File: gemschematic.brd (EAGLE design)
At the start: 90.2 x 61.9 mm, 57 parts, among them J1 USB, J3 QWIIC, J5 U.FL, Q1 2N3904, Q2 BSS138, Q3 MBT3904DW1T1, U1 ESP-WROOM-32NARROW, U2 AP2112K-3.3, U3 3.3V, U4 RFM96W, U5 CH340C, U6 BMP180, U7 STM32L073RZT6, X1 GPS_PA1010D

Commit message: Add files via upload
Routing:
- net GND: track 0.00 -> 423.1 mm, vias 0 -> 9
- net 3.3V: track 0.00 -> 279.9 mm
- net SDA: track 0.00 -> 189.3 mm, vias 0 -> 11
- net VCC: track 0.00 -> 183.9 mm, vias 0 -> 8
- net SCL: track 0.00 -> 179.1 mm, vias 0 -> 10
- net RESET: track 0.00 -> 171.9 mm, vias 0 -> 6
- net MISO: track 0.00 -> 156.4 mm, vias 0 -> 5
- net IO25: track 0.00 -> 154.6 mm, vias 0 -> 3
- net RFM_DIO2/32: track 0.00 -> 142.8 mm, vias 0 -> 2
- net SCK: track 0.00 -> 141.3 mm, vias 0 -> 7
- net IO27: track 0.00 -> 140.8 mm, vias 0 -> 5
- net ANT: track 0.00 -> 127.0 mm, vias 0 -> 5
- net MOSI: track 0.00 -> 125.1 mm, vias 0 -> 6
- net RXI: track 0.00 -> 120.5 mm, vias 0 -> 5
- net TXO: track 0.00 -> 114.0 mm, vias 0 -> 4
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
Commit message: Add files via upload
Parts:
- removed B1: (no value), microbuilder:CR1220-2
- removed C1: 0.1uF, microbuilder:0603-NO
- removed C2, C3: 10uF, microbuilder:0805-NO
- removed C4: 10uF, SparkFun-Capacitors:0603
- removed C5, C6: 0.1uF, SparkFun-Capacitors:0603
- removed C7, C8: 1.0uF, SparkFun-Capacitors:0603
- removed C9: 4.7uF, SparkFun-Capacitors:0603
- removed CONN3, CONN4: STEMMA_I2C_QT, microbuilder:JST_SH4
- removed D1: GREEN, microbuilder:CHIPLED_0603_NOOUTLINE
- removed D2: 1N4148, microbuilder:SOD-323
- removed D3: RED, microbuilder:CHIPLED_0603_NOOUTLINE
- removed D4: RED, SparkFun-LED:LED-0603
- removed D5: GREEN, SparkFun-LED:LED-0603
- removed FB1: FERRITE, microbuilder:0805-NO
- removed J1: USB, SparkFun-Connectors:USB-MICROB-PTH-MILL
- removed J3: QWIIC, SparkFun-Connectors:1X04_1MM_RA
- removed J4: (no value), SparkFun-Connectors:1X08_NO_SILK
- removed J5: U.FL, SparkFun-Connectors:U.FL
- removed J8: (no value), SparkFun-Connectors:1X01_NO_SILK
- removed J9: (no value), SparkFun-Connectors:1X10_NO_SILK
- removed JP1: DNP, SparkFun-Connectors:MOLEX-1X3
- removed JP2: (no value), SparkFun-Connectors:SCREWTERMINAL-3.5MM-3_LOCK.007S
- removed JP3, JP4: (no value), microbuilder:1X06_ROUND_70
- removed JP5: (no value), pinhead:1X02
- removed PULLUP: 10k, adafruit:0204V
- removed Q1: 2N3904, SparkFun-DiscreteSemi:SOT23-3
- removed Q2: BSS138, microbuilder:SOT363
- removed Q3: MBT3904DW1T1, esp32-thing-temp:SC70-6
- removed R10, R17, R18, R6, R8: 10k, SparkFun-Resistors:0603
- removed R2: 100, SparkFun-Resistors:0603-RES
- removed R3, R4, R5: 10K, microbuilder:RESPACK_4X0603
- removed R7, R9: 1k, SparkFun-Resistors:0603
- removed S1: RESET, SparkFun-Switches:TACTILE_SWITCH_SMD_4.6X2.8MM
- removed S2: 0, SparkFun-Switches:TACTILE_SWITCH_SMD_4.6X2.8MM
- removed U1: ESP-WROOM-32NARROW, esp32_lora_gateway:ESP-WROOM-32-NARROW
- removed U2: AP2112K-3.3, microbuilder:SOT23-5
- removed U3: 3.3V, SparkFun-IC-Power:SOT23-5
- removed U4: RFM96W, SparkX:RFM95/96/97/98W
- removed U5: CH340C, SparkFun-IC-Comms:SO016
- removed U6: BMP180, BMP180:BMP180
- removed X1: GPS_PA1010D, microbuilder:GPS_PA1010D
- added BARO: 22-23-2041, con-molex:22-23-2041
- added BLUETOOTH: 87438-06, con-molex:87438-06
- added GPS1JUMPER, GPS2JUMPER: (no value), microbuilder:1X06_ROUND_70
- added LDRJUMPER: (no value), pinhead:1X02
- added LORA1JUMPER: (no value), SparkFun-Connectors:1X08_NO_SILK
- added LORA2JUMPER: (no value), SparkFun-Connectors:1X10_NO_SILK
- added LORANT: (no value), SparkFun-Connectors:1X01_NO_SILK
- added PULLUP1, PULLUP2: 4.7k, adafruit:0204V
- added SOILJUMPER: (no value), SparkFun-Connectors:SCREWTERMINAL-3.5MM-3_LOCK.007S
- DS18B20: value 22-23-2041 -> (none); device con-molex:22-23-2041 -> adafruit:1X03
- R1: value 10k -> 270; device SparkFun-Resistors:0603-RES -> adafruit:0204V
- moved DHT22 65.6 mm to (19.1, 21.6)
- moved U7 55.1 mm to (64.8, 22.9)
- moved DS18B20 54.8 mm to (19.1, 45.7)
- moved R1 36.6 mm to (63.5, 63.5), turned to 90 degrees
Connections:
- removed net !DTR: Q3.1, R17.1, U5.13
- removed net !RTS: Q3.4, R18.1, U5.14
- removed net 0: Q3.6, R10.1, S2.3, S2.4, U1.25
- removed net D+: J1.D+, U5.5
- removed net D-: J1.D-, U5.6
- removed net DATA: DHT22.2, DS18B20.2, PULLUP.1
- removed net DHT22: U7.9
- removed net IO17: R9.1, U1.28
- removed net MISO: J4.2, U1.14, U4.MISO, U7.53
- removed net MOSI: J4.1, U1.16, U4.MOSI, U7.52
- removed net N$10: Q3.5, R17.2
- removed net N$12: Q3.2, R18.2
- removed net N$2: D1.C, R4.6
- removed net N$3: D3.C, R4.7, R4.8
- removed net N$4: D4.C, R7.2
- removed net N$5: D5.A, R9.2
- removed net OUT: FB1.1, U2.5
- removed net PC5: JP5.1
- removed net PF0: U6.6
- removed net PF1: U6.5
- removed net PHOTO: U7.8
- removed net PROBE1: Q1.1
- removed net PROBE2: R2.1
- removed net RFM_CS: U1.27, U4.NSS
- removed net RFM_DIO1/33: U1.9, U4.DIO1
- removed net RFM_DIO2/32: U1.8, U4.DIO2
- removed net RFM_INT/26: U1.11, U4.DIO0
- removed net RFM_RST: R8.1, U4.!RESET
- removed net RXI_3V: D2.A, R3.5, X1.5
- removed net SCK: J4.3, U1.13, U4.SCK, U7.51
- removed net SCL_3V: Q2.1, R5.7, X1.2
- removed net SDA_3V: Q2.4, R5.5, X1.1
- removed net SHIELD: J1.SHIELD, J1.SHIELD10, J1.SHIELD2, J1.SHIELD3, J1.SHIELD4, J1.SHIELD5, J1.SHIELD6, J1.SHIELD7, J1.SHIELD8, J1.SHIELD9
- removed net SIG: JP1.3, JP2.1, Q1.2, R1.2
- removed net SOIL: U7.11
- removed net TEMP: U7.10
- removed net USART_RX: U7.17
- removed net USART_TX: U7.16
- removed net VBACKUP: B1.+, X1.9
- removed net VDDIO: U6.3
- removed net V_USB: C7.1, J1.VBUS, U3.1, U3.3
- new net BTRX: BLUETOOTH.2, U7.51
- new net BTTX: BLUETOOTH.3, U7.15
- new net GPSRX: GPS2JUMPER.4, U7.42
- new net GPSTX: GPS2JUMPER.5, U7.43
- new net MISOLORA: LORA1JUMPER.2, U7.53
- new net MOSILORA: LORA1JUMPER.1, U7.52
- new net PA0LDR: LDRJUMPER.1, R1.2, U7.14
- new net PC1DHT: DHT22.2, PULLUP1.1, U7.9
- new net PC2DS18B20: DS18B20.2, PULLUP2.1, U7.10
- new net PC3SOIL: SOILJUMPER.1, U7.11
- new net SCKLORA: LORA1JUMPER.3, U7.37
- new net SCLBARO: BARO.3, U7.58
- new net SDABARO: BARO.4, U7.59
- new net VIN: BARO.1
- net !RESET: now also GPS1JUMPER.6; no longer JP3.6, X1.6
- net 1PPS: now also GPS2JUMPER.2; no longer D3.A, JP4.2, X1.3
- net 3.3V: now also GPS1JUMPER.2; no longer C1.1, C3.1, C4.1, C5.1, C8.1, C9.1, D1.A, D4.A, FB1.2, J3.2, J4.7, JP3.2, Q2.2, Q2.5, R10.2, R3.4, R5.2, R5.4, R6.2, R8.2, U1.2, U3.5, U4.3.3V, U5.16, U5.4, U7.13, X1.10
- net ANT: now also LORANT.1; no longer J5.FEED, J8.1, U4.ANT
- net GND: now also BARO.2, BLUETOOTH.5, DS18B20.3, GPS1JUMPER.3, GPS2JUMPER.1, LORA1JUMPER.8, LORA2JUMPER.10, SOILJUMPER.2; no longer B1.-, C1.2, C2.2, C3.2, C4.2, C5.2, C6.2, C7.2, C8.2, C9.2, CONN3.1, CONN4.1, D5.C, DS18B20.4, J1.GND, J3.1, J4.8, J5.1, J5.2, J9.10, JP1.2, JP2.2, JP3.3, JP4.1, R4.1, R4.2, R4.3, R7.1, S1.1, S1.2, S2.1, S2.2, U1.1, U1.15, U1.38, U1.GND, U2.2, U3.2, U4.GND@1, U4.GND@2, U4.GND@3, U5.1, U6.7, X1.7
- net IO18: now also LORA2JUMPER.5; no longer J9.5, U1.30
- net IO19: now also LORA2JUMPER.6; no longer J9.6, U1.31
- net IO23: now also LORA2JUMPER.7; no longer J9.7, U1.37
- net IO25: now also LORA1JUMPER.5; no longer J4.5, U1.10
- net IO27: now also LORA1JUMPER.4; no longer J4.4, U1.12
- net IO4: now also LORA2JUMPER.3; no longer J9.3, U1.26
- net IO5: now also LORA2JUMPER.4; no longer J9.4, U1.29
- net RESET: now also LORA1JUMPER.6; no longer C6.1, J4.6, Q3.3, R6.1, S1.3, S1.4, U1.3
- net RXI: now also LORA2JUMPER.8; no longer D2.C, J9.8, JP4.4, U1.34, U5.2
- net SCL: now also LORA2JUMPER.2; no longer CONN3.4, CONN4.4, J3.4, J9.2, JP3.4, Q2.6, R5.8, U1.36, U7.59
- net SDA: now also LORA2JUMPER.1; no longer CONN3.3, CONN4.3, J3.3, J9.1, JP3.5, Q2.3, R5.6, U1.33, U7.58
- net TXO: now also LORA2JUMPER.9; no longer J9.9, JP4.5, U1.35, U5.3, X1.4
- net VCC: now also BLUETOOTH.4, GPS1JUMPER.1, GPS2JUMPER.3, LDRJUMPER.2, LORA1JUMPER.7, PULLUP1.2, PULLUP2.2, SOILJUMPER.3, U7.13; no longer C2.1, CONN3.2, CONN4.2, JP1.1, JP2.3, JP3.1, JP4.3, PULLUP.2, Q1.3, R2.2, R5.1, R5.3, U2.1, U2.3
- net VDD: no longer U6.2
- net WAKEUP: now also GPS2JUMPER.6; no longer JP4.6, X1.8
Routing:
- net 3.3V: track 279.9 -> 0.00 mm
- net GND: track 423.1 -> 201.9 mm, vias 9 -> 1
- net SDA: track 189.3 -> 0.00 mm, vias 11 -> 0
- net SCL: track 179.1 -> 0.00 mm, vias 10 -> 0
- net RESET: track 171.9 -> 0.00 mm, vias 6 -> 0
- net MISO: track 156.4 -> 0.00 mm, vias 5 -> 0
- net IO25: track 154.6 -> 0.00 mm, vias 3 -> 0
- net RFM_DIO2/32: track 142.8 -> 0.00 mm, vias 2 -> 0
- net SCK: track 141.3 -> 0.00 mm, vias 7 -> 0
- net IO27: track 140.8 -> 0.00 mm, vias 5 -> 0
- net ANT: track 127.0 -> 0.00 mm, vias 5 -> 0
- net MOSI: track 125.1 -> 0.00 mm, vias 6 -> 0
- net RXI: track 120.5 -> 0.00 mm, vias 5 -> 0
- net TXO: track 114.0 -> 0.00 mm, vias 4 -> 0
- net PA0LDR: track 0.00 -> 106.7 mm, vias 0 -> 1
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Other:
- board size 90.2 x 61.9 mm -> 88.9 x 100 mm
- board text added: "UCSB 2022 GEM"

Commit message: Add files via upload
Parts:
- added POWER: (no value), pinhead:1X02
- added STLINK: 22-23-2041, con-molex:22-23-2041
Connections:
- removed net VIN: BARO.1
- new net SWCLK: STLINK.3, U7.49
- new net SWIO: STLINK.2, U7.46
- net GND: now also POWER.2, STLINK.4
- net MISOLORA: now also U7.22; no longer U7.53
- net MOSILORA: now also U7.23; no longer U7.52
- net SCKLORA: now also U7.21; no longer U7.37
- net VCC: now also BARO.1, POWER.1, STLINK.1
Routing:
- net VCC: track 191.0 -> 241.9 mm
- net GND: track 201.9 -> 251.9 mm, vias 1 -> 2
- net SWIO: track 0.00 -> 39.9 mm, vias 0 -> 1
- net SWCLK: track 0.00 -> 36.0 mm, vias 0 -> 1
- net MISOLORA: track 77.7 -> 107.0 mm, vias 1 -> 3
- net MOSILORA: track 79.2 -> 107.4 mm, vias 1 -> 3
- net VDD: track 22.2 -> 17.2 mm, vias 0 -> 2

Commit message: Add files via upload
added butons
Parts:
- added LEDRESISTOR: 510 Ohm, adafruit:0204V
- added RESETBUTTON, USERBUTTON: (no value), adafruit:B3F-40XX
- added USERLED: (no value), adafruit:LED3MM
- BLUETOOTH: value 87438-06 -> (none); device con-molex:87438-06 -> adafruit:1X06
- STLINK: value 22-23-2041 -> (none); device con-molex:22-23-2041 -> adafruit:1X06
- moved R1 70.1 mm to (22.9, 6.35), turned to 180 degrees
- moved PULLUP1 46.8 mm to (27.9, 21.6), turned to 0 degrees
- moved PULLUP2 36.4 mm to (26.7, 45.7), turned to 180 degrees
- moved BLUETOOTH 10.2 mm to (43.2, 34.3)
- moved STLINK 9.16 mm to (35.6, 5.08)
- moved LDRJUMPER 1.80 mm to (16.5, 6.35)
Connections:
- removed net !RESET: GPS1JUMPER.6
- removed net 3.3V: GPS1JUMPER.2
- removed net ANT: LORANT.1
- removed net IO18: LORA2JUMPER.5
- removed net IO19: LORA2JUMPER.6
- removed net IO23: LORA2JUMPER.7
- removed net IO25: LORA1JUMPER.5
- removed net IO27: LORA1JUMPER.4
- removed net IO4: LORA2JUMPER.3
- removed net IO5: LORA2JUMPER.4
- removed net MISOLORA: LORA1JUMPER.2, U7.22
- removed net MOSILORA: LORA1JUMPER.1, U7.23
- removed net RESET: LORA1JUMPER.6
- removed net RXI: LORA2JUMPER.8
- removed net SCKLORA: LORA1JUMPER.3, U7.21
- removed net SCL: LORA2JUMPER.2
- removed net SDA: LORA2JUMPER.1
- removed net SWCLK: STLINK.3, U7.49
- removed net SWIO: STLINK.2, U7.46
- removed net TXO: LORA2JUMPER.9
- removed net WAKEUP: GPS2JUMPER.6
- new net LED: LEDRESISTOR.2, U7.21
- new net N$1: LEDRESISTOR.1, USERLED.K
- new net NRST: RESETBUTTON.3, RESETBUTTON.4, STLINK.5, U7.7
- new net SWCLKSTLINK: STLINK.2, U7.49
- new net SWDIOSTLINK: STLINK.4, U7.46
- new net SWOSTLINK: STLINK.6, U7.55
- new net USERBUTTON: U7.2, USERBUTTON.3, USERBUTTON.4
- net GND: now also RESETBUTTON.1, RESETBUTTON.2, STLINK.3, U7.60, USERBUTTON.1, USERBUTTON.2; no longer STLINK.4
- net VCC: no longer STLINK.1
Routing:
- net MOSILORA: track 107.4 -> 0.00 mm, vias 3 -> 0
- net MISOLORA: track 107.0 -> 0.00 mm, vias 3 -> 0
- net NRST: track 0.00 -> 90.0 mm
- net SCKLORA: track 86.0 -> 0.00 mm, vias 1 -> 0
- net LED: track 0.00 -> 60.6 mm, vias 0 -> 1
- net SWCLKSTLINK: track 0.00 -> 57.0 mm, vias 0 -> 1
- net SCLBARO: track 47.6 -> 103.8 mm, vias 2 -> 1
- net PA0LDR: track 106.7 -> 52.3 mm, vias 1 -> 0
- net SWDIOSTLINK: track 0.00 -> 48.0 mm
- net USERBUTTON: track 0.00 -> 43.3 mm
- net SWIO: track 39.9 -> 0.00 mm, vias 1 -> 0
- net SWOSTLINK: track 0.00 -> 37.0 mm
- net SWCLK: track 36.0 -> 0.00 mm, vias 1 -> 0
- net PC2DS18B20: track 85.0 -> 52.5 mm, vias 3 -> 1
- net GND: track 251.9 -> 281.3 mm, vias 2 -> 1
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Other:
- board text added: "UCSB 2022 GEM Version 1.0"
- board text removed: "UCSB 2022 GEM"

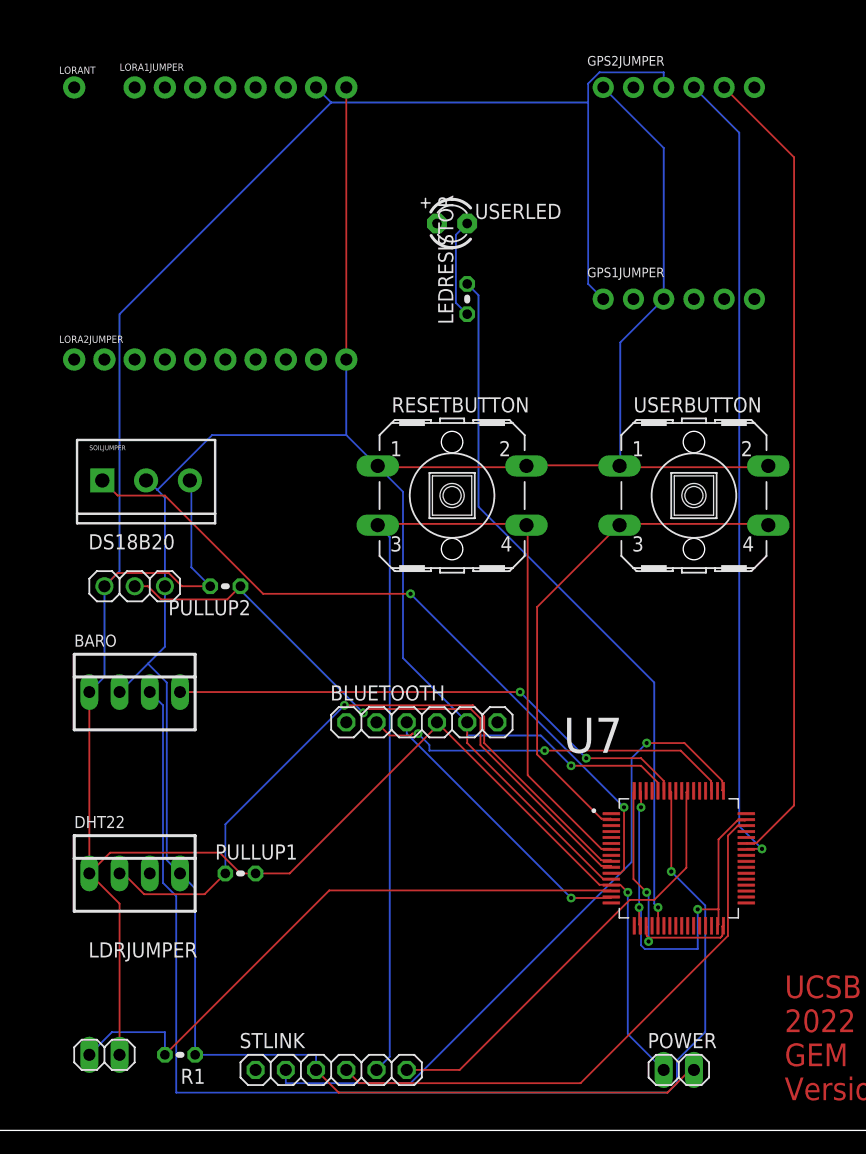
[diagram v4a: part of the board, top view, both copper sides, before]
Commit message: added smd parts
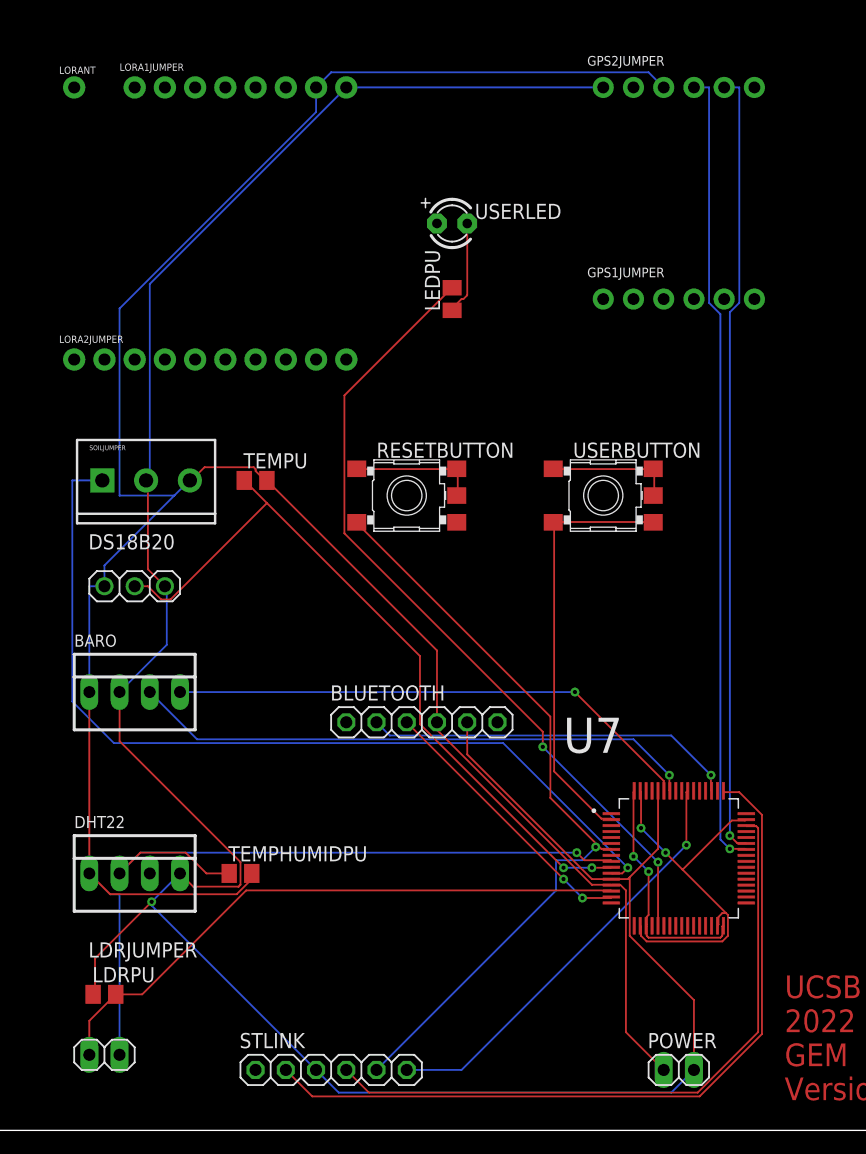
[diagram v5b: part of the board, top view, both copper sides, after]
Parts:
- removed LEDRESISTOR: 510 Ohm, adafruit:0204V
- removed PULLUP1, PULLUP2: 4.7k, adafruit:0204V
- removed R1: 270, adafruit:0204V
- added LDRPU: 270, adafruit:M0805
- added LEDPU: 510 Ohm, adafruit:M0805
- added TEMPHUMIDPU, TEMPU: 4.7k, adafruit:M0805
- RESETBUTTON, USERBUTTON: value (none) -> SKHMPSE010; device adafruit:B3F-40XX -> switch:SKHMPXE010
- moved USERBUTTON 7.62 mm to (58.4, 53.3)
- moved RESETBUTTON 3.81 mm to (41.9, 53.3)
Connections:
- new net N$2: USERBUTTON.1, USERBUTTON.2, USERBUTTON.5
- new net N$4: RESETBUTTON.1, RESETBUTTON.2, RESETBUTTON.5
- net GND: now also LDRPU.1; no longer GPS1JUMPER.3, LORA2JUMPER.10, R1.1, RESETBUTTON.1, RESETBUTTON.2, USERBUTTON.1, USERBUTTON.2
- net LED: now also LEDPU.2; no longer LEDRESISTOR.2
- net N$1: now also LEDPU.1; no longer LEDRESISTOR.1
- net NRST: no longer RESETBUTTON.4
- net PA0LDR: now also LDRPU.2; no longer R1.2
- net PC1DHT: now also TEMPHUMIDPU.1; no longer PULLUP1.1
- net PC2DS18B20: now also TEMPU.1; no longer PULLUP2.1
- net VCC: now also TEMPHUMIDPU.2, TEMPU.2; no longer GPS1JUMPER.1, PULLUP1.2, PULLUP2.2
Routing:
- net GND: track 281.3 -> 222.0 mm
- net SCLBARO: track 103.8 -> 47.9 mm
- net NRST: track 90.0 -> 64.7 mm, vias 0 -> 1
- net VCC: track 233.1 -> 217.7 mm, vias 1 -> 0
- net PC3SOIL: track 61.6 -> 75.1 mm, vias 2 -> 1
- net N$4: track 0.00 -> 10.8 mm
- net N$2: track 0.00 -> 10.8 mm
- net PC2DS18B20: track 52.5 -> 62.6 mm, vias 1 -> 2
- net SWCLKSTLINK: track 57.0 -> 65.6 mm, vias 1 -> 0
- net SWDIOSTLINK: track 48.0 -> 55.7 mm
- net LED: track 60.6 -> 68.3 mm, vias 1 -> 2
- net USERBUTTON: track 43.3 -> 35.9 mm
- net PC1DHT: track 57.8 -> 53.0 mm
- net VSS: track 35.0 -> 32.4 mm, vias 3 -> 2
- net GPSTX: track 68.1 -> 66.1 mm, vias 0 -> 1
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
